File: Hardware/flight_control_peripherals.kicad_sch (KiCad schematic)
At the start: 17 parts, among them J10 Conn_01x06, J11 Micro_SD_Card_Det1, J5 Conn_01x10, J6 Conn_02x10_Odd_Even, J7 Conn_01x04, J8 Conn_01x04, J9 Conn_02x06_Odd_Even, U13 W25N01GVZEIG_TR, U14 24CW1280T-I/OT, U15 PCA9685PW_118

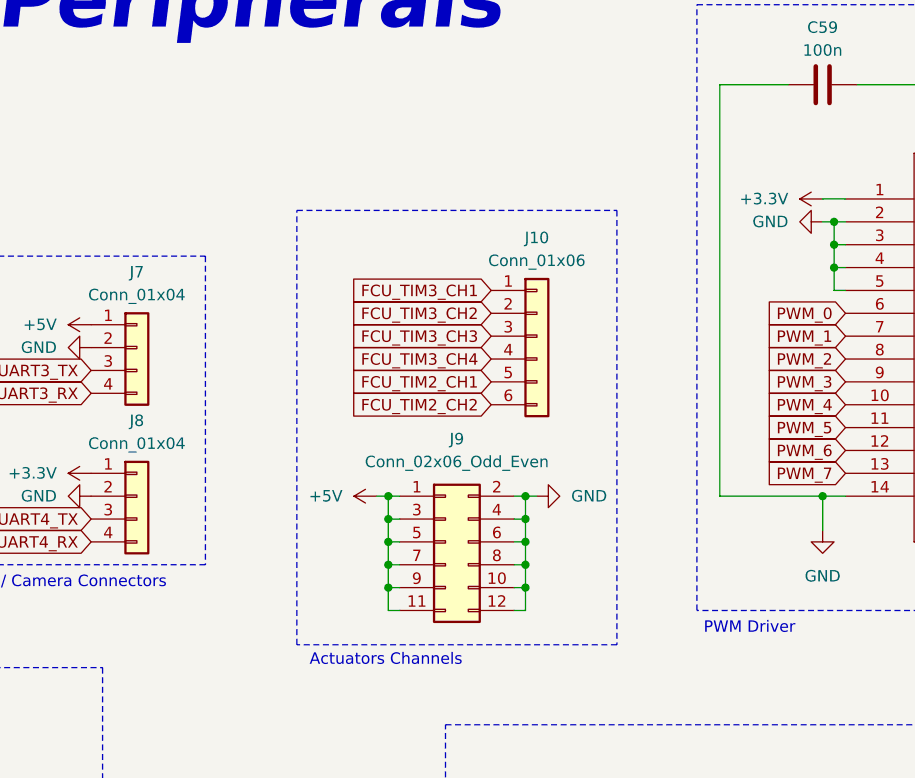
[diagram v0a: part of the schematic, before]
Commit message: hardware version 0.1.2, minor improvements and footprint selection (missing some gnss and bulk regulator components
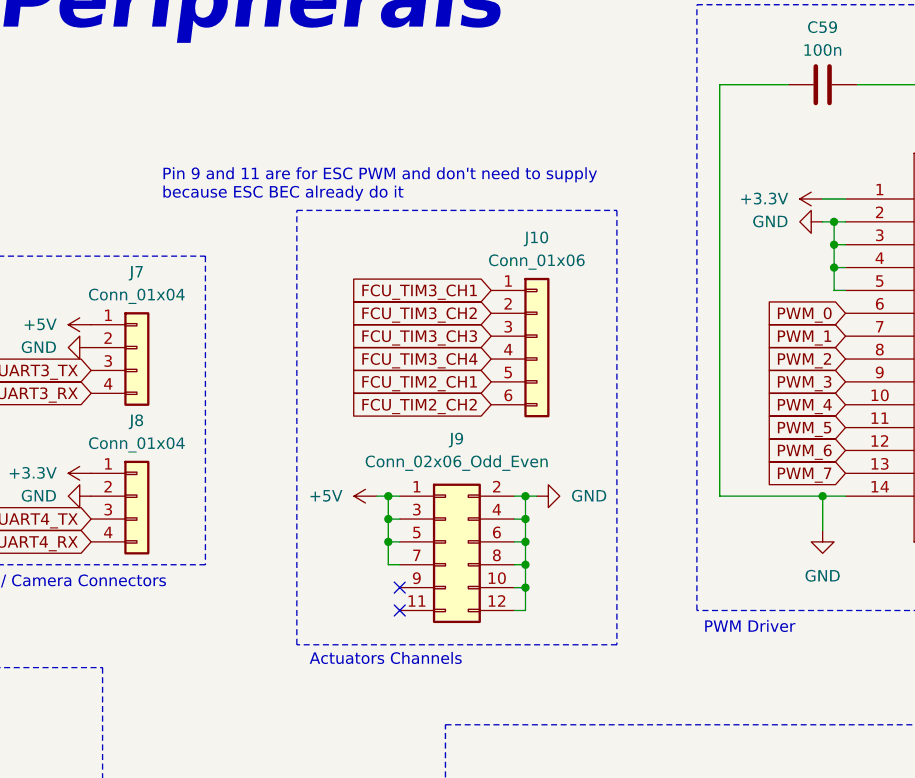
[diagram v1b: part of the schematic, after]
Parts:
- J10: footprint (none) -> Connector_PinHeader_2.54mm:PinHeader_1x06_P2.54mm_Vertical
- J11: footprint (none) -> Connector_Card:microSD_HC_Hirose_DM3AT-SF-PEJM5
- J5: footprint (none) -> Connector_PinHeader_2.54mm:PinHeader_1x10_P2.54mm_Vertical
- J6: footprint (none) -> Connector_PinHeader_2.54mm:PinHeader_2x10_P2.54mm_Vertical
- J7, J8: footprint (none) -> Connector_JST:JST_PH_S4B-PH-K_1x04_P2.00mm_Horizontal
- J9: footprint (none) -> Connector_PinHeader_2.54mm:PinHeader_2x06_P2.54mm_Vertical
- R33, R34: footprint (none) -> Resistor_SMD:R_0603_1608Metric_Pad0.98x0.95mm_HandSolder
- U13: footprint W25N01GVZEIG_TR:SON127P800X600X80-9N -> Aircraft_Footprints:SON127P800X600X80-9N
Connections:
- net +5V: no longer J9.11 (Pin_11), J9.9 (Pin_9)
- no-connect marks 10 -> 12
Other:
- note added: "Pin 9 and 11 are for ESC PWM and don't need to supply because ESC BEC already do it"
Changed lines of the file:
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@@
 	(title_block
 		(title "Flight Control Unit - Peripherals")
-		(rev "0.1.0")
+		(rev "0.1.2")
 		(company "Breno Soares Alves")
 	)
@@
 		)
 	)
+	(text "Pin 9 and 11 are for ESC PWM and don't need to supply\nbecause ESC BEC already do it"
+		(exclude_from_sim no)
+		(at 136.144 40.386 0)
+		(effects
+			(font
+				(size 1.27 1.27)
+			)
+			(justify left)
+		)
+	)
 	(text "Radio / Camera Connectors"
 		(exclude_from_sim no)
@@
 	)
 	(junction
-		(at 161.29 85.09)
-		(diameter 0)
-		(color 0 0 0 0)
-	)
-	(junction
 		(at 161.29 77.47)
 		(diameter 0)
@@
 	)
 	(junction
-		(at 161.29 82.55)
-		(diameter 0)
-		(color 0 0 0 0)
-	)
-	(junction
 		(at 210.82 49.53)
 		(diameter 0)
@@
 	)
 	(no_connect
+		(at 162.56 85.09)
+	)
+	(no_connect
+		(at 162.56 87.63)
+	)
+	(no_connect
 		(at 257.81 49.53)
 	)
@@
 	(wire
 		(pts
-			(xy 161.29 82.55) (xy 161.29 85.09)
-		)
-		(stroke
-			(width 0)
-			(type default)
-		)
-	)
-	(wire
-		(pts
 			(xy 257.81 54.61) (xy 260.35 54.61)
 		)
@@
 	(wire
 		(pts
-			(xy 161.29 87.63) (xy 162.56 87.63)
-		)
-		(stroke
-			(width 0)
-			(type default)
-		)
-	)
-	(wire
-		(pts
 			(xy 106.68 106.68) (xy 97.79 106.68)
 		)
@@
 	(wire
 		(pts
-			(xy 161.29 85.09) (xy 162.56 85.09)
-		)
-		(stroke
-			(width 0)
-			(type default)
-		)
-	)
-	(wire
-		(pts
 			(xy 175.26 74.93) (xy 176.53 74.93)
 		)
@@
 	(wire
 		(pts
-			(xy 161.29 85.09) (xy 161.29 87.63)
-		)
-		(stroke
-			(width 0)
-			(type default)
-		)
-	)
-	(wire
-		(pts
 			(xy 181.61 119.38) (xy 181.61 120.65)
 		)
@@
 			)
 		)
-		(property "Footprint" ""
+		(property "Footprint" "Connector_PinHeader_2.54mm:PinHeader_1x06_P2.54mm_Vertical"
 			(at 177.8 57.15 0)
 			(effects
@@
 			)
 		)
-		(property "Footprint" ""
+		(property "Footprint" "Resistor_SMD:R_0603_1608Metric_Pad0.98x0.95mm_HandSolder"
 			(at 104.902 111.76 90)
 			(effects
@@
 			)
 		)
-		(property "Footprint" ""
+		(property "Footprint" "Connector_PinHeader_2.54mm:PinHeader_1x10_P2.54mm_Vertical"
 			(at 52.07 62.23 0)
 			(effects
@@
 			)
 		)
-		(property "Footprint" ""
+		(property "Footprint" "Resistor_SMD:R_0603_1608Metric_Pad0.98x0.95mm_HandSolder"
 			(at 96.012 111.76 90)
 			(effects
@@
 			)
 		)
-		(property "Footprint" ""
+		(property "Footprint" "Connector_JST:JST_PH_S4B-PH-K_1x04_P2.00mm_Horizontal"
 			(at 133.35 74.93 0)
 			(effects
@@
 			)
 		)
-		(property "Footprint" ""
+		(property "Footprint" "Connector_Card:microSD_HC_Hirose_DM3AT-SF-PEJM5"
 			(at 281.94 106.68 0)
 			(effects
@@
 			)
 		)
-		(property "Footprint" ""
+		(property "Footprint" "Connector_PinHeader_2.54mm:PinHeader_2x06_P2.54mm_Vertical"
 			(at 167.64 80.01 0)
 			(effects
@@
 			)
 		)
-		(property "Footprint" ""
+		(property "Footprint" "Connector_PinHeader_2.54mm:PinHeader_2x10_P2.54mm_Vertical"
 			(at 76.2 62.23 0)
 			(effects
@@
 			)
 		)
-		(property "Footprint" "W25N01GVZEIG_TR:SON127P800X600X80-9N"
+		(property "Footprint" "Aircraft_Footprints:SON127P800X600X80-9N"
 			(at 73.66 114.3 0)
 			(effects
@@
 			)
 		)
-		(property "Footprint" ""
+		(property "Footprint" "Connector_JST:JST_PH_S4B-PH-K_1x04_P2.00mm_Horizontal"
 			(at 133.35 58.42 0)
 			(effects

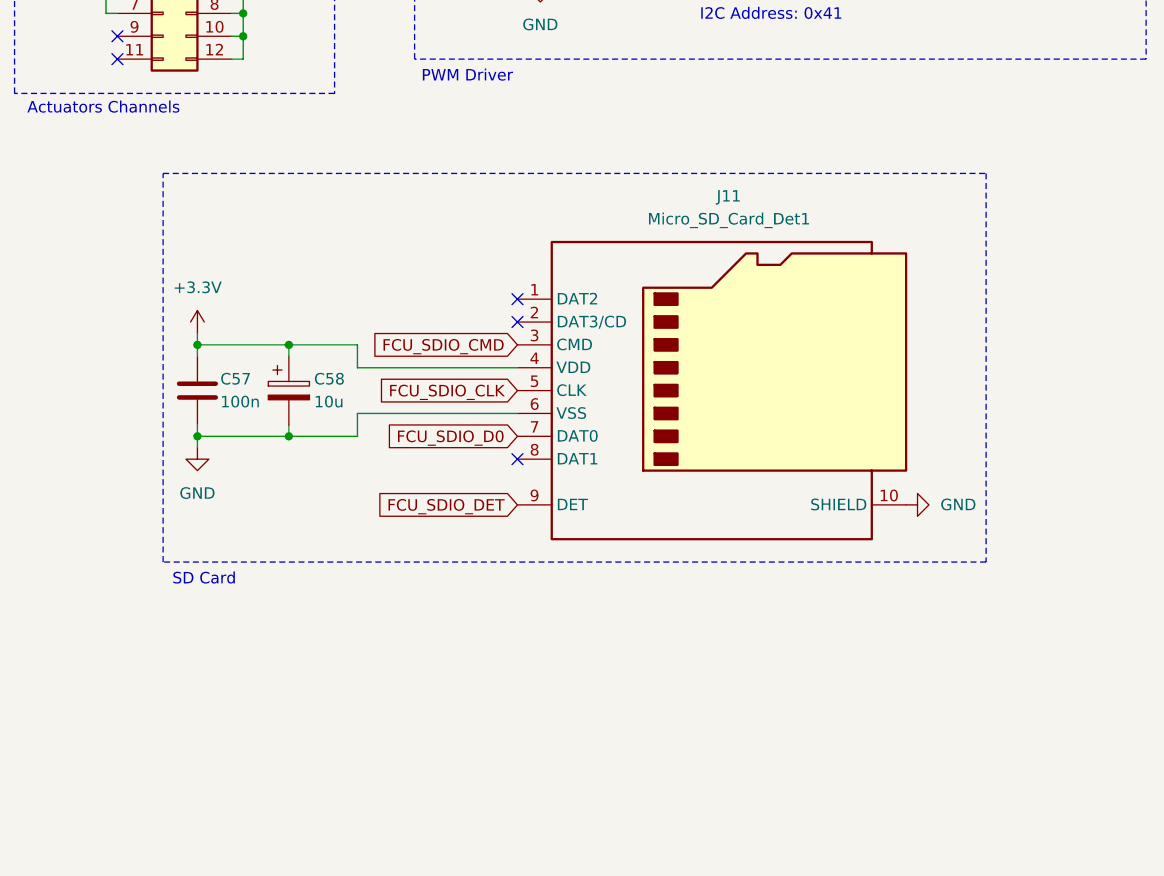
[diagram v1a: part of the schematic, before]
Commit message: board placement, no trails, just pain
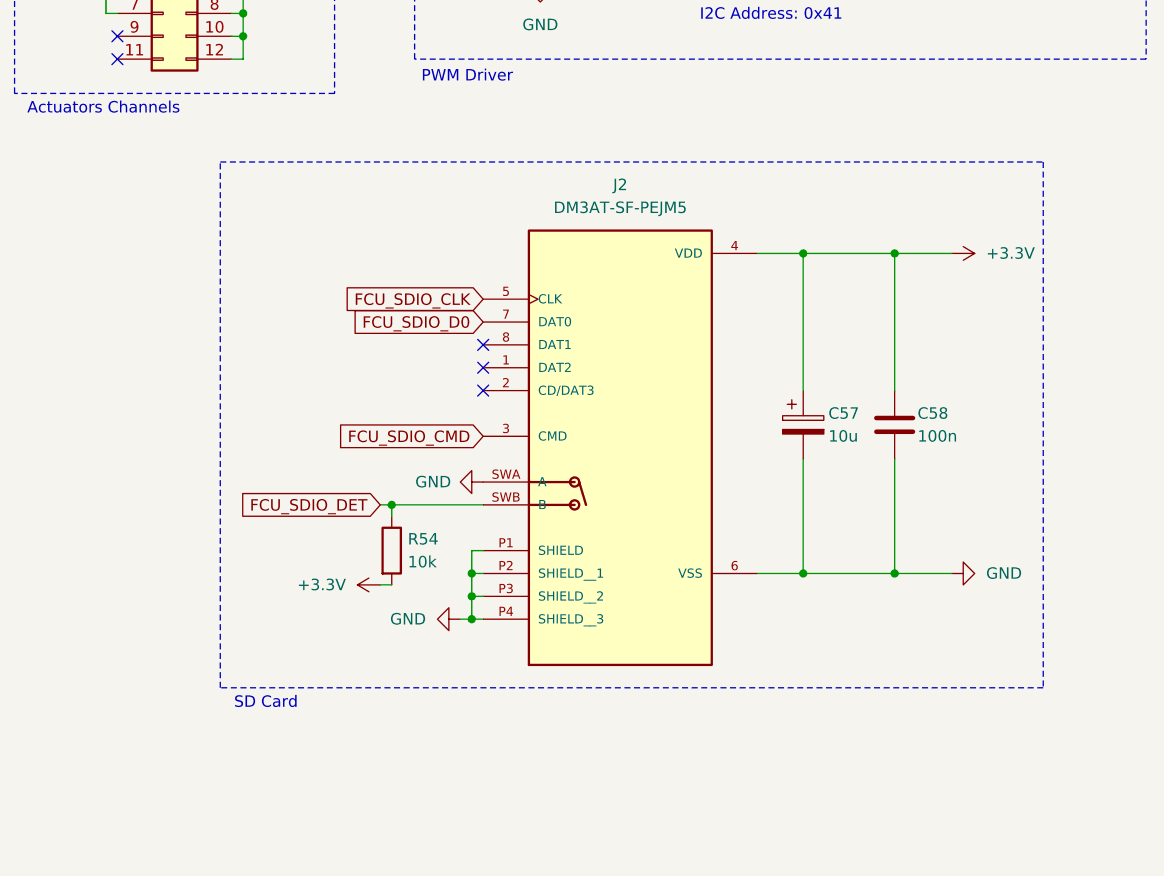
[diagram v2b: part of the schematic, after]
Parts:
- removed C57: 100n, Capacitor_SMD:C_0603_1608Metric, symbol Device:C
- removed C58: 10u, Capacitor_Tantalum_SMD:CP_EIA-1608-08_AVX-J, symbol Device:C_Polarized
- removed J11: Micro_SD_Card_Det1, Connector_Card:microSD_HC_Hirose_DM3AT-SF-PEJM5, symbol Connector:Micro_SD_Card_Det1
- added C57: 10u, Capacitor_SMD:C_1206_3216Metric_Pad1.33x1.80mm_HandSolder, symbol Device:C_Polarized
- added C58: 100n, Capacitor_SMD:C_0603_1608Metric, symbol Device:C
- added J2: DM3AT-SF-PEJM5, Aircraft_Footprints:HRS_DM3AT-SF-PEJM5, symbol Aircraft_Components:DM3AT-SF-PEJM5
- added R54: 10k, Resistor_SMD:R_0603_1608Metric_Pad0.98x0.95mm_HandSolder, symbol Device:R
- C55, C56, C59: Digikey_Link (none) -> https://www.digikey.com.br/pt/products/detail/kemet/C0603C1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; MPN (none) -> C0603C104K8RACTU
- J10, J5, J6, J9: MPN (none) -> Generic 2.54mm PinHeader; now left out of the parts list
- J7, J8: Digikey_Link (none) -> https://www.digikey.com.br/pt/products/detail/jst-sales-ame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; MPN (none) -> S4B-PH-K-S
- R33, R34: Digikey_Link (none) -> https://www.digikey.com.br/pt/products/detail/yageo/RC0603F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; MPN (none) -> RC0603FR-0710KL
- U13: Digikey_Link (none) -> https://www.digikey.com.br/pt/products/detail/winbond-elect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; MPN (none) -> W25N01GVZEIG-TR
- U14: Digikey_Link (none) -> https://www.digikey.com.br/pt/products/detail/microchip-tec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; MPN (none) -> 24CW1280T-I/OT
- U15: Digikey_Link (none) -> https://www.digikey.com.br/pt/products/detail/nxp-usa-inc/p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; MPN (none) -> PCA9685PW,118
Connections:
- net +3.3V: now also C57.1, C58.1, J2.4 (VDD), R54.2
- net FCU_SDIO_CLK: now also J2.5 (CLK)
- net FCU_SDIO_CMD: now also J2.3 (CMD)
- net FCU_SDIO_D0: now also J2.7 (DAT0)
- net FCU_SDIO_DET: now also J2.SWB (B), R54.1
- net GND: now also C57.2, C58.2, J2.6 (VSS), J2.P1 (SHIELD), J2.P2 (SHIELD__1), J2.P3 (SHIELD__2), J2.P4 (SHIELD__3), J2.SWA (A)
